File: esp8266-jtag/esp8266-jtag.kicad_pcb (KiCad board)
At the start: 2 copper layers, 30.5 x 28.4 mm, 14 parts, among them CON1 jtag, P1 CONN_01X08, P2 flash, P3 CONN_01X08, P4 CONN_01X02, U1 ESP-12E

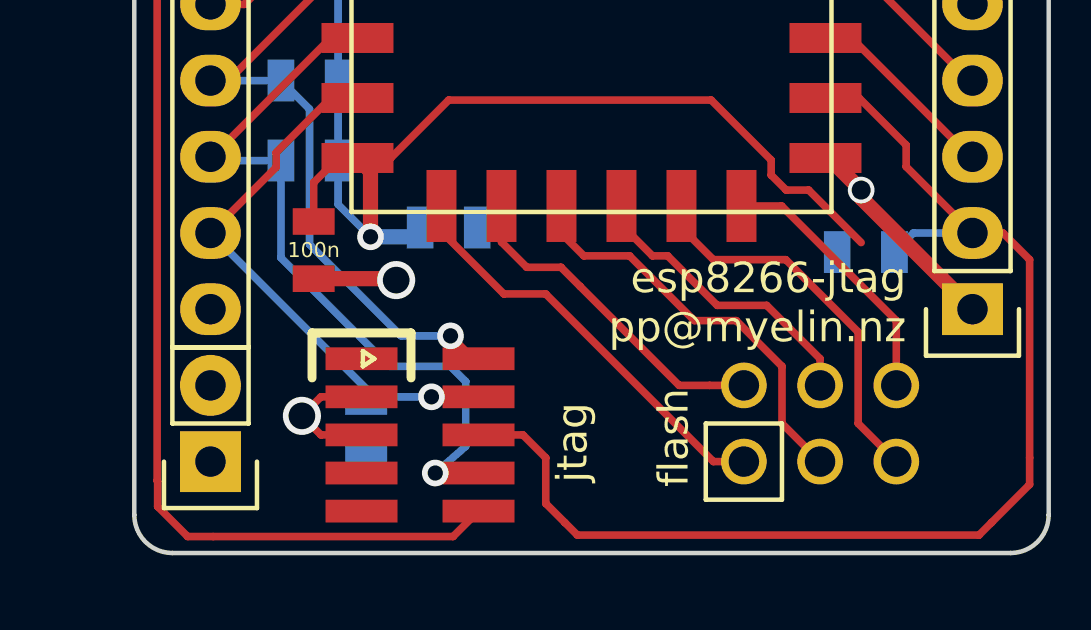
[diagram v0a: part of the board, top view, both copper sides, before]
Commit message: Reduced the size of a pad that looked too close to another pad, and moved a resistor to not look offset from the text
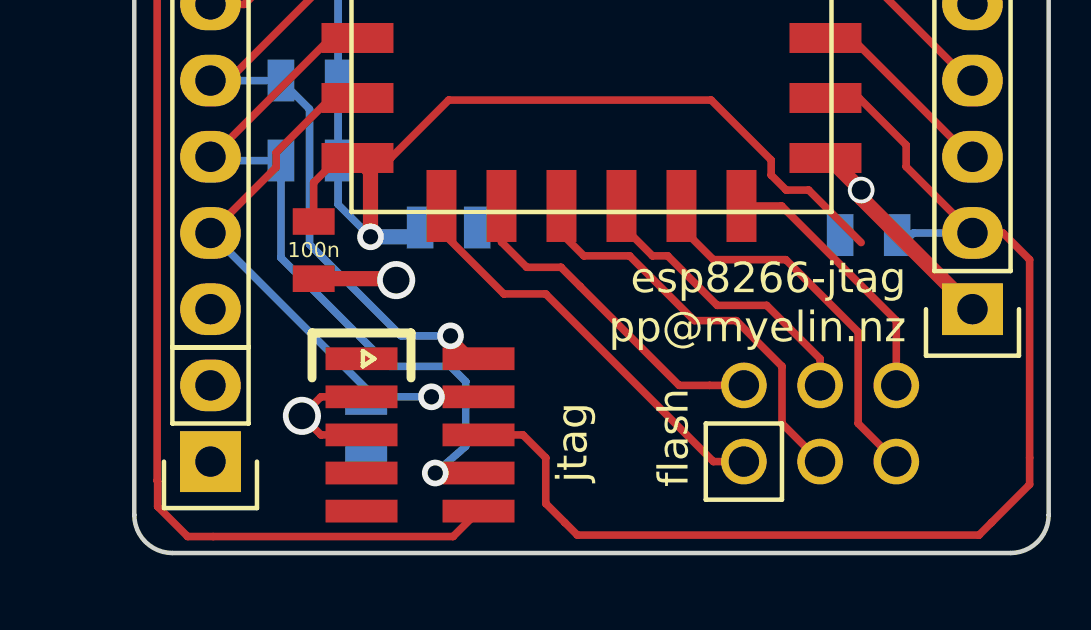
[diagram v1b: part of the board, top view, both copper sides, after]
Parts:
- moved R3 0.57 mm to (152.8, 106.8)
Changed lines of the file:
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@@
   (layers
     (0 F.Cu signal)
-    (31 B.Cu signal hide)
+    (31 B.Cu signal)
     (32 B.Adhes user)
     (33 F.Adhes user)
@@
     (mod_text_size 1 1)
     (mod_text_width 0.15)
-    (pad_size 1.524 1.524)
-    (pad_drill 0.762)
+    (pad_size 2.032 1.7272)
+    (pad_drill 1.016)
     (pad_to_mask_clearance 0.2)
     (aux_axis_origin 0 0)
-    (visible_elements 7FFF7FFF)
+    (visible_elements 7FFFFFFF)
     (pcbplotparams
       (layerselection 0x010fc_80000001)
@@
   )
   (module myelin-kicad:R0805_nosilkscreen (layer B.Cu)
-    (at 152.654 107.315)
+    (at 152.75 106.75)
     (descr "SM0805 module from KiCad stdlib, modified by Phillip Pearson to have less annoying silkscreen")
     (attr smd)
@@
     (pad 1 thru_hole rect (at 0 0 180) (size 2.032 2.032) (drill 1.016) (layers *.Cu *.Mask F.SilkS)
       (net 5 /3v3))
-    (pad 2 thru_hole oval (at 0 2.54 180) (size 2.032 2.032) (drill 1.016) (layers *.Cu *.Mask F.SilkS)
+    (pad 2 thru_hole oval (at 0 2.54 180) (size 2.032 1.7272) (drill 1.016) (layers *.Cu *.Mask F.SilkS)
       (net 7 /gnd))
     (model Pin_Headers.3dshapes/Pin_Header_Straight_1x02.wrl
